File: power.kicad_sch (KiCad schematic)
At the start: 16 parts, among them U3 SY8120IABC, U4 SY8120IABC

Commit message: Finish preliminary charger and logic schematic
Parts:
- added R42: 100k, Resistor_SMD:R_0402_1005Metric, symbol Device:R_Small
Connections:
- net GND: now also R42.2
- net LED_EN: now also R42.1
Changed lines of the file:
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@@
   (junction (at 139.7 90.17) (diameter 0) (color 0 0 0 0)
   )
+  (junction (at 101.6 128.27) (diameter 0) (color 0 0 0 0)
+  )
   (junction (at 139.7 121.92) (diameter 0) (color 0 0 0 0)
   )
@@
     (stroke (width 0) (type default))
   )
+  (wire (pts (xy 101.6 128.27) (xy 113.03 128.27))
+    (stroke (width 0) (type default))
+  )
   (wire (pts (xy 144.78 121.92) (xy 153.67 121.92))
     (stroke (width 0) (type default))
@@
     (stroke (width 0) (type default))
   )
-  (wire (pts (xy 99.06 128.27) (xy 113.03 128.27))
+  (wire (pts (xy 99.06 128.27) (xy 101.6 128.27))
     (stroke (width 0) (type default))
   )
@@
   )
   (wire (pts (xy 123.19 115.57) (xy 121.92 115.57))
+    (stroke (width 0) (type default))
+  )
+  (wire (pts (xy 101.6 128.27) (xy 101.6 129.54))
     (stroke (width 0) (type default))
   )
@@
         (path "/20b2a5b0-0a80-4b97-84d4-d5290b2926e5/ec178502-7b55-459c-9ab3-b7e99f46d37d"
           (reference "C22") (unit 1)
+        )
+      )
+    )
+  )
+  (symbol (lib_id "Device:R_Small") (at 101.6 132.08 0) (mirror y) (unit 1)
+    (in_bom yes) (on_board yes) (dnp no)
+    (property "Reference" "R42" (at 100.1014 130.8679 0)
+      (effects (font (size 1.27 1.27)) (justify left))
+    )
+    (property "Value" "100k" (at 100.1014 133.2921 0)
+      (effects (font (size 1.27 1.27)) (justify left))
+    )
+    (property "Footprint" "Resistor_SMD:R_0402_1005Metric" (at 101.6 132.08 0)
+      (effects (font (size 1.27 1.27)) hide)
+    )
+    (property "Datasheet" "~" (at 101.6 132.08 0)
+      (effects (font (size 1.27 1.27)) hide)
+    )
+    (property "LCSC" "C25741" (at 101.6 132.08 0)
+      (effects (font (size 1.27 1.27)) hide)
+    )
+    (pin "1")
+    (pin "2")
+    (instances
+      (project "blinkekatze"
+        (path "/20b2a5b0-0a80-4b97-84d4-d5290b2926e5/ec178502-7b55-459c-9ab3-b7e99f46d37d"
+          (reference "R42") (unit 1)
         )
       )
@@
         )
       )
+    )
+  )
+  (symbol (lib_id "power:GND") (at 101.6 134.62 0) (unit 1)
+    (in_bom yes) (on_board yes) (dnp no) (fields_autoplaced)
+    (property "Reference" "#PWR0102" (at 101.6 140.97 0)
+      (effects (font (size 1.27 1.27)) hide)
+    )
+    (property "Value" "GND" (at 101.6 138.7531 0)
+      (effects (font (size 1.27 1.27)))
+    )
+    (property "Footprint" "" (at 101.6 134.62 0)
+      (effects (font (size 1.27 1.27)) hide)
+    )
+    (property "Datasheet" "" (at 101.6 134.62 0)
+      (effects (font (size 1.27 1.27)) hide)
+    )
+    (pin "1")
+    (instances
+      (project "blinkekatze"
+        (path "/20b2a5b0-0a80-4b97-84d4-d5290b2926e5/ec178502-7b55-459c-9ab3-b7e99f46d37d"
+          (reference "#PWR0102") (unit 1)
+        )
+      )

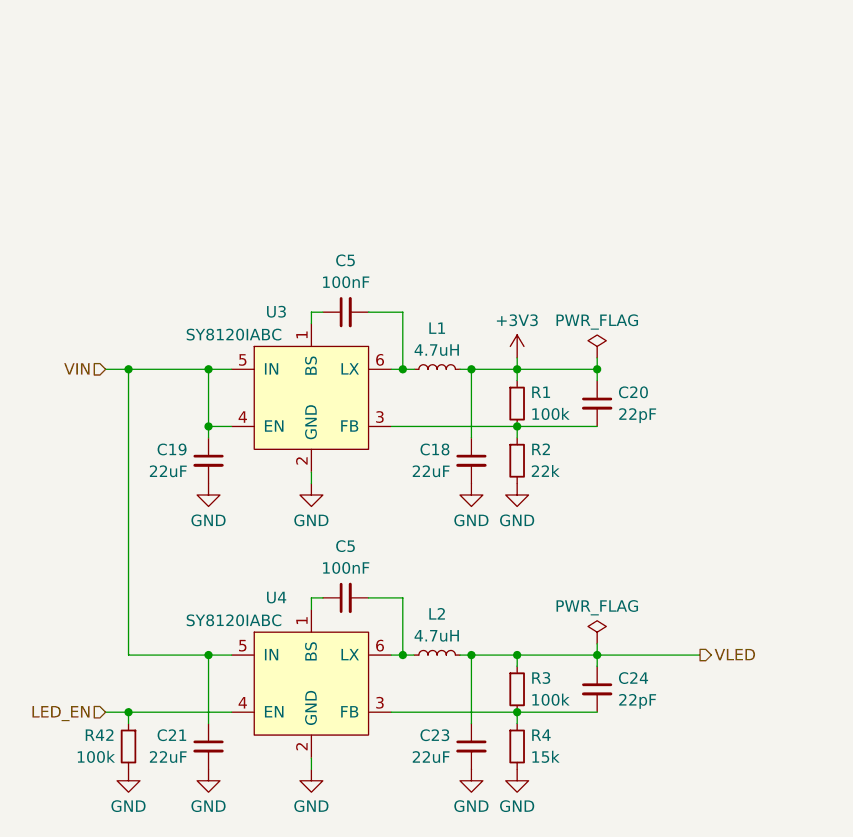
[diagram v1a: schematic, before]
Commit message: Finish rough layout
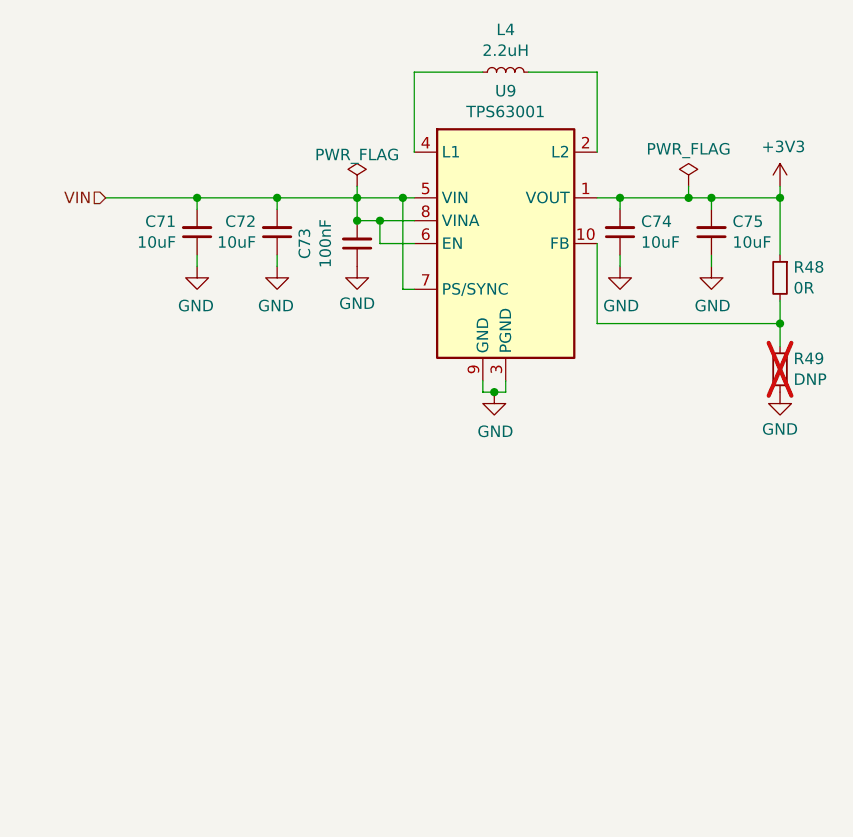
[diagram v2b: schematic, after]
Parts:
- removed C18, C19, C21, C23: 22uF, Capacitor_SMD:C_0805_2012Metric, symbol Device:C_Small
- removed C20, C24: 22pF, Capacitor_SMD:C_0402_1005Metric, symbol Device:C_Small
- removed C5 (x2): 100nF, Capacitor_SMD:C_0402_1005Metric, symbol Device:C_Small
- removed L1, L2: 4.7uH, Inductor_SMD:L_Taiyo-Yuden_MD-3030, symbol Device:L_Small
- removed R1, R3, R42: 100k, Resistor_SMD:R_0402_1005Metric, symbol Device:R_Small
- removed R2: 22k, Resistor_SMD:R_0402_1005Metric, symbol Device:R_Small
- removed R4: 15k, Resistor_SMD:R_0402_1005Metric, symbol Device:R_Small
- removed U3, U4: SY8120IABC, Package_TO_SOT_SMD:SOT-23-6, symbol Regulator_Switching_Silergy:SY8113B
- added C71, C72, C74, C75: 10uF, Capacitor_SMD:C_0402_1005Metric, symbol Device:C_Small
- added C73: 100nF, Capacitor_SMD:C_0402_1005Metric, symbol Device:C_Small
- added L4: 2.2uH, Inductor_SMD:L_Taiyo-Yuden_MD-4040, symbol Device:L_Small
- added R48: 0R, Resistor_SMD:R_0402_1005Metric, symbol Device:R_Small
- added R49: DNP, Resistor_SMD:R_0402_1005Metric, symbol Device:R_Small
- added U9: TPS63001, Package_Texas:Texas_DRC0010J_ThermalVias.3, symbol Regulator_Switching:TPS63001
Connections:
- net +3V3: now also C74.2, C75.2, R48.1, U9.1 (VOUT)
- net GND: now also C71.1, C72.1, C73.1, C74.1, C75.1, R49.2, U9.11 (PGND), U9.3 (PGND), U9.9 (GND)
- net VIN: now also C71.2, C72.2, C73.2, U9.5 (VIN), U9.6 (EN), U9.7 (PS/SYNC), U9.8 (VINA)
- new net: L4.1, U9.4 (L1)
- new net: L4.2, U9.2 (L2)
- new net: R48.2, R49.1, U9.10 (FB)
